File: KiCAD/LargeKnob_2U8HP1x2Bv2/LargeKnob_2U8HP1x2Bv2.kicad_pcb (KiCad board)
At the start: 2 copper layers, 40.3 x 84 mm, 6 parts

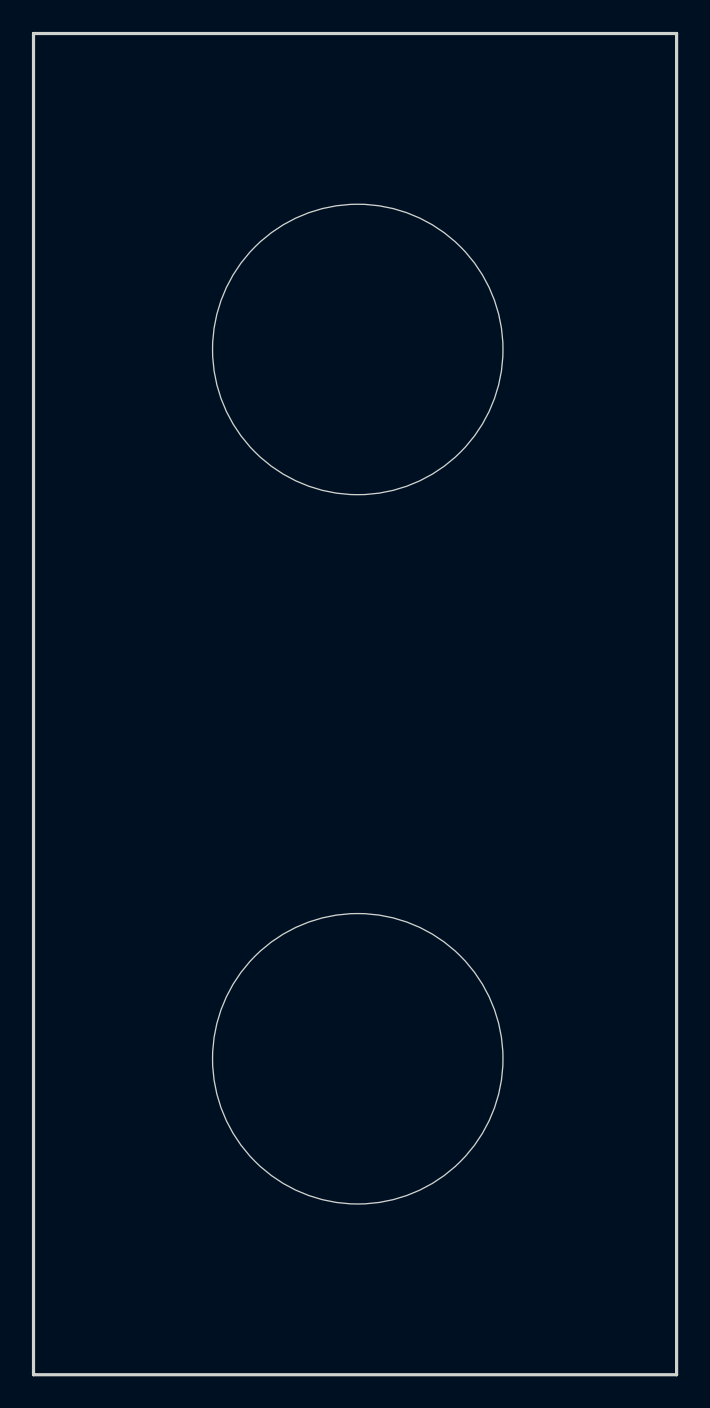
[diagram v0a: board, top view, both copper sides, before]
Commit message: updated all modules to use plated through-holes wherever possible
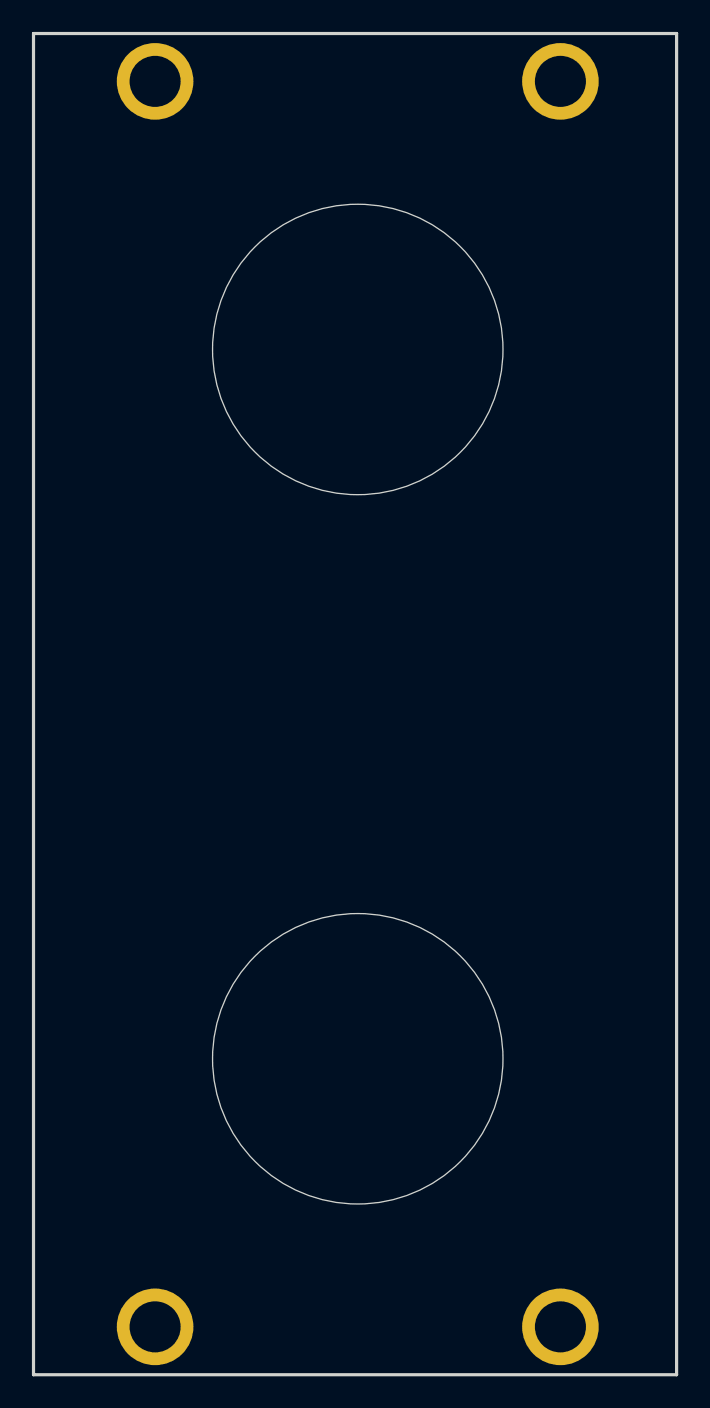
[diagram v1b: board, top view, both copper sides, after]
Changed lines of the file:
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@@
 			)
 		)
-		(pad "" np_thru_hole oval
+		(pad "" thru_hole circle
 			(at 0 0)
-			(size 4.34 3.2)
-			(drill oval 4.34 3.2)
+			(size 4.8 4.8)
+			(drill 3.2)
 			(layers "*.Cu" "*.Mask")
+			(remove_unused_layers no)
 		)
 		(embedded_fonts no)
@@
 			)
 		)
-		(pad "" np_thru_hole oval
+		(pad "" thru_hole circle
 			(at 0 0)
-			(size 4.34 3.2)
-			(drill oval 4.34 3.2)
+			(size 4.8 4.8)
+			(drill 3.2)
 			(layers "*.Cu" "*.Mask")
+			(remove_unused_layers no)
 		)
 		(embedded_fonts no)
@@
 			)
 		)
-		(pad "" np_thru_hole oval
+		(pad "" thru_hole circle
 			(at 0 0)
-			(size 4.34 3.2)
-			(drill oval 4.34 3.2)
+			(size 4.8 4.8)
+			(drill 3.2)
 			(layers "*.Cu" "*.Mask")
+			(remove_unused_layers no)
 		)
 		(embedded_fonts no)
@@
 			)
 		)
-		(pad "" np_thru_hole oval
+		(pad "" thru_hole circle
 			(at 0 0)
-			(size 4.34 3.2)
-			(drill oval 4.34 3.2)
+			(size 4.8 4.8)
+			(drill 3.2)
 			(layers "*.Cu" "*.Mask")
+			(remove_unused_layers no)
 		)
 		(embedded_fonts no)
